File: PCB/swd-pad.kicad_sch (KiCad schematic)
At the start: 10 parts, among them J7 OroConn6p

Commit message: re-annotate schematic
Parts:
- renumbered D12 to D4, D13 to D5, D15 to D7
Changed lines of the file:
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@@
   (symbol (lib_id "SamacSys_Parts:RCLAMP3552T.TNT") (at 135.89 115.57 180) (unit 1)
     (in_bom yes) (on_board yes) (dnp no) (fields_autoplaced)
-    (property "Reference" "D13" (at 125.73 107.5309 0)
+    (property "Reference" "D5" (at 125.73 107.5309 0)
       (effects (font (size 1.27 1.27)))
     )
@@
       (project "OroLink"
         (path "/e89dcd22-1250-4a5b-b778-1c95a0dd623d/259c9346-7ad9-40c3-9e14-9b19afc78ddf"
-          (reference "D13") (unit 1)
+          (reference "D5") (unit 1)
         )
       )
@@
         )
         (path "/e89dcd22-1250-4a5b-b778-1c95a0dd623d/259c9346-7ad9-40c3-9e14-9b19afc78ddf"
-          (reference "D14") (unit 1)
+          (reference "D6") (unit 1)
         )
       )
@@
   (symbol (lib_id "power:GNDPWR") (at 111.125 115.57 0) (unit 1)
     (in_bom yes) (on_board yes) (dnp no)
-    (property "Reference" "#PWR069" (at 111.125 120.65 0)
+    (property "Reference" "#PWR072" (at 111.125 120.65 0)
       (effects (font (size 1.27 1.27)) hide)
     )
@@
       (project "OroLink"
         (path "/e89dcd22-1250-4a5b-b778-1c95a0dd623d/259c9346-7ad9-40c3-9e14-9b19afc78ddf"
-          (reference "#PWR069") (unit 1)
+          (reference "#PWR072") (unit 1)
         )
       )
@@
         )
         (path "/e89dcd22-1250-4a5b-b778-1c95a0dd623d/259c9346-7ad9-40c3-9e14-9b19afc78ddf"
-          (reference "DBG42") (unit 1)
+          (reference "DBG10") (unit 1)
         )
       )
@@
         )
         (path "/e89dcd22-1250-4a5b-b778-1c95a0dd623d/259c9346-7ad9-40c3-9e14-9b19afc78ddf"
-          (reference "#PWR070") (unit 1)
+          (reference "#PWR073") (unit 1)
         )
       )
@@
         )
         (path "/e89dcd22-1250-4a5b-b778-1c95a0dd623d/259c9346-7ad9-40c3-9e14-9b19afc78ddf"
-          (reference "DBG43") (unit 1)
+          (reference "DBG11") (unit 1)
         )
       )
@@
   (symbol (lib_id "power:GND") (at 170.18 82.55 0) (unit 1)
     (in_bom yes) (on_board yes) (dnp no) (fields_autoplaced)
-    (property "Reference" "#PWR071" (at 170.18 88.9 0)
+    (property "Reference" "#PWR074" (at 170.18 88.9 0)
       (effects (font (size 1.27 1.27)) hide)
     )
@@
       (project "OroLink"
         (path "/e89dcd22-1250-4a5b-b778-1c95a0dd623d/259c9346-7ad9-40c3-9e14-9b19afc78ddf"
-          (reference "#PWR071") (unit 1)
+          (reference "#PWR074") (unit 1)
         )
       )
@@
         )
         (path "/e89dcd22-1250-4a5b-b778-1c95a0dd623d/259c9346-7ad9-40c3-9e14-9b19afc78ddf"
-          (reference "DBG41") (unit 1)
+          (reference "DBG9") (unit 1)
         )
       )
@@
   (symbol (lib_id "power:GNDPWR") (at 188.595 115.57 0) (unit 1)
     (in_bom yes) (on_board yes) (dnp no)
-    (property "Reference" "#PWR072" (at 188.595 120.65 0)
+    (property "Reference" "#PWR075" (at 188.595 120.65 0)
       (effects (font (size 1.27 1.27)) hide)
     )
@@
       (project "OroLink"
         (path "/e89dcd22-1250-4a5b-b778-1c95a0dd623d/259c9346-7ad9-40c3-9e14-9b19afc78ddf"
-          (reference "#PWR072") (unit 1)
+          (reference "#PWR075") (unit 1)
         )
       )
@@
   (symbol (lib_id "SamacSys_Parts:RCLAMP3552T.TNT") (at 163.83 113.03 0) (unit 1)
     (in_bom yes) (on_board yes) (dnp no) (fields_autoplaced)
-    (property "Reference" "D15" (at 173.99 107.5309 0)
+    (property "Reference" "D7" (at 173.99 107.5309 0)
       (effects (font (size 1.27 1.27)))
     )
@@
       (project "OroLink"
         (path "/e89dcd22-1250-4a5b-b778-1c95a0dd623d/259c9346-7ad9-40c3-9e14-9b19afc78ddf"
-          (reference "D15") (unit 1)
+          (reference "D7") (unit 1)
         )
       )
@@
         )
         (path "/e89dcd22-1250-4a5b-b778-1c95a0dd623d/259c9346-7ad9-40c3-9e14-9b19afc78ddf"
-          (reference "DBG39") (unit 1)
+          (reference "DBG7") (unit 1)
         )
       )
@@
         )
         (path "/e89dcd22-1250-4a5b-b778-1c95a0dd623d/259c9346-7ad9-40c3-9e14-9b19afc78ddf"
-          (reference "DBG40") (unit 1)
+          (reference "DBG8") (unit 1)
         )
       )
@@
   (symbol (lib_id "power:+5V") (at 86.995 82.55 0) (unit 1)
     (in_bom yes) (on_board yes) (dnp no) (fields_autoplaced)
-    (property "Reference" "#PWR068" (at 86.995 86.36 0)
+    (property "Reference" "#PWR071" (at 86.995 86.36 0)
       (effects (font (size 1.27 1.27)) hide)
     )
@@
       (project "OroLink"
         (path "/e89dcd22-1250-4a5b-b778-1c95a0dd623d/259c9346-7ad9-40c3-9e14-9b19afc78ddf"
-          (reference "#PWR068") (unit 1)
+          (reference "#PWR071") (unit 1)
         )
       )
@@
   (symbol (lib_id "SamacSys_Parts:RFU02VSM8STR") (at 92.71 82.55 0) (unit 1)
     (in_bom yes) (on_board yes) (dnp no)
-    (property "Reference" "D12" (at 100.33 76.835 0)
+    (property "Reference" "D4" (at 100.33 76.835 0)
       (effects (font (size 1.27 1.27)))
     )
@@
       (project "OroLink"
         (path "/e89dcd22-1250-4a5b-b778-1c95a0dd623d/259c9346-7ad9-40c3-9e14-9b19afc78ddf"
-          (reference "D12") (unit 1)
-        )
-      )
+          (reference "D4") (unit 1)
+        )
+      )

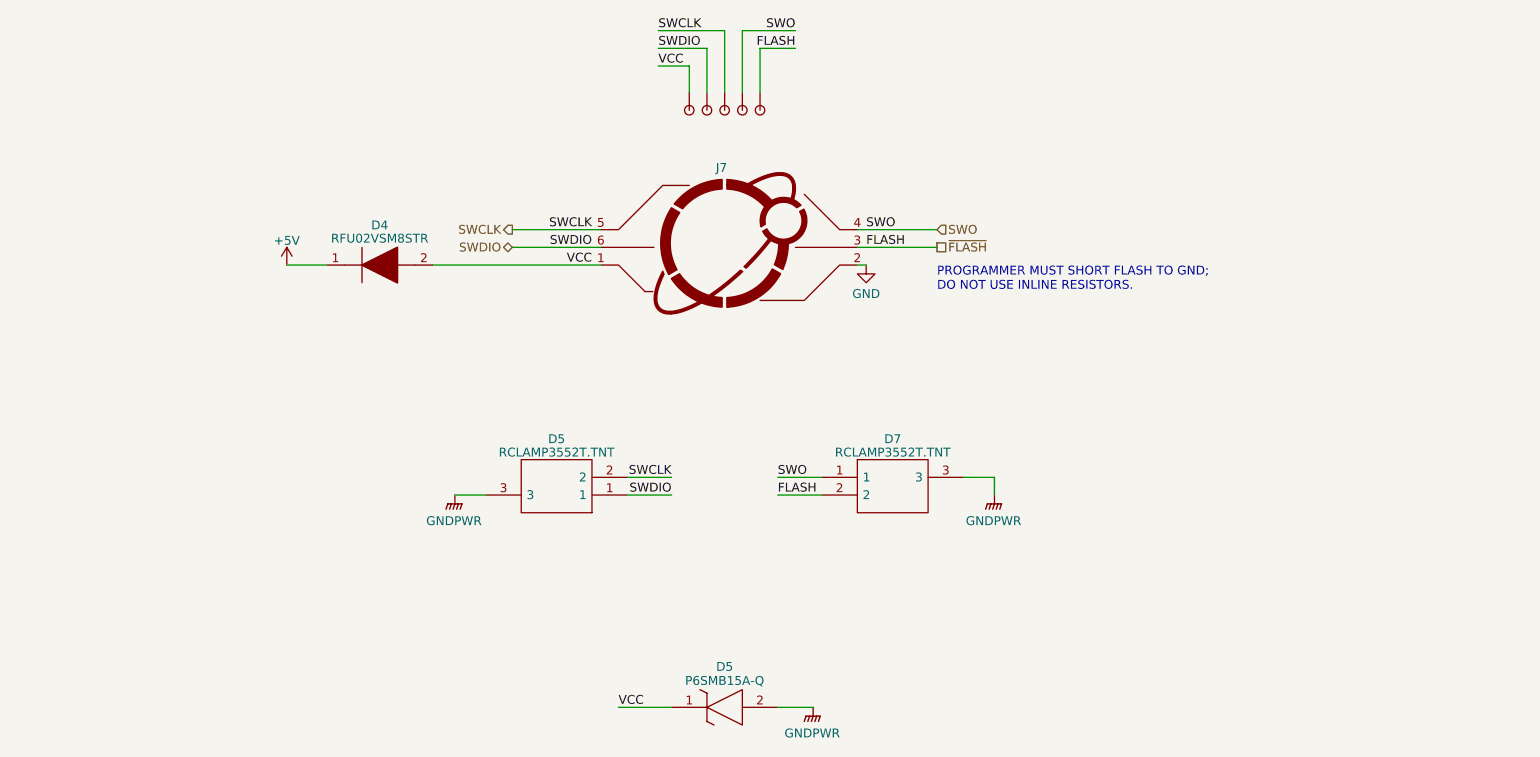
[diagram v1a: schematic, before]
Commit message: add pullup/down resistors and fix oro 6p lines with boot1/0
closes #24
closes #21
closes #15
closes #12
closes #6
closes #3
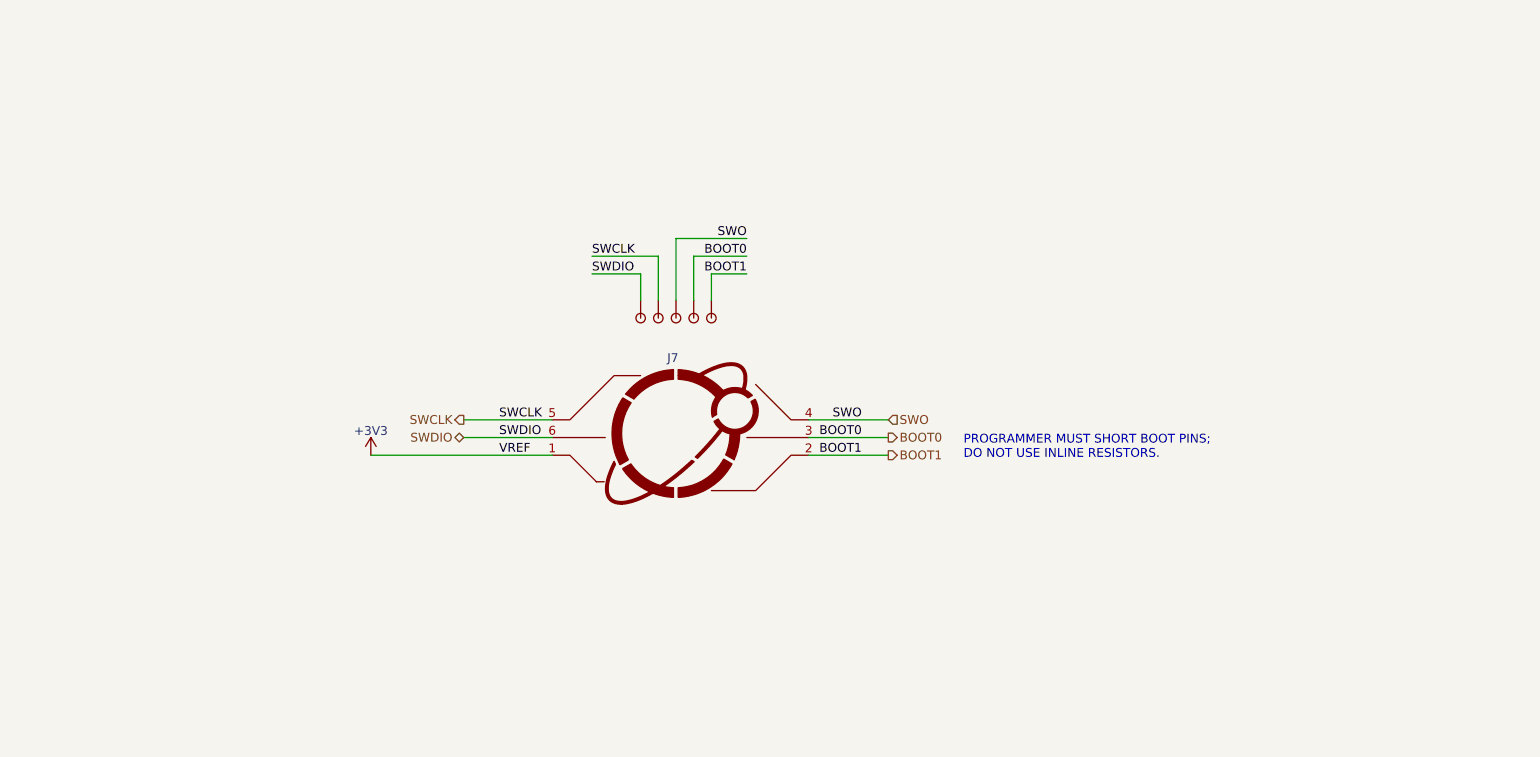
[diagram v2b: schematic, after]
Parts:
- removed D4: RFU02VSM8STR, SODFL2514X80N, symbol SamacSys_Parts:RFU02VSM8STR
- removed D5, D7: RCLAMP3552T.TNT, RCLAMP3552TTNT, symbol SamacSys_Parts:RCLAMP3552T.TNT
- removed D5: P6SMB15A-Q, DIOM5436X244N, symbol SamacSys_Parts:P6SMB15A-Q
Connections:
- net GND renamed BOOT1
- net BOOT1: now also DBG1.1
- net VCC renamed +3V3
- net +3V3: no longer DBG1.1
- net ~{FLASH} renamed BOOT0
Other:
- note added: "PROGRAMMER MUST SHORT BOOT PINS; DO NOT USE INLINE RESISTORS."
- note removed: "PROGRAMMER MUST SHORT FLASH TO GND; DO NOT USE INLINE RESISTORS."
- moved on the sheet: J7

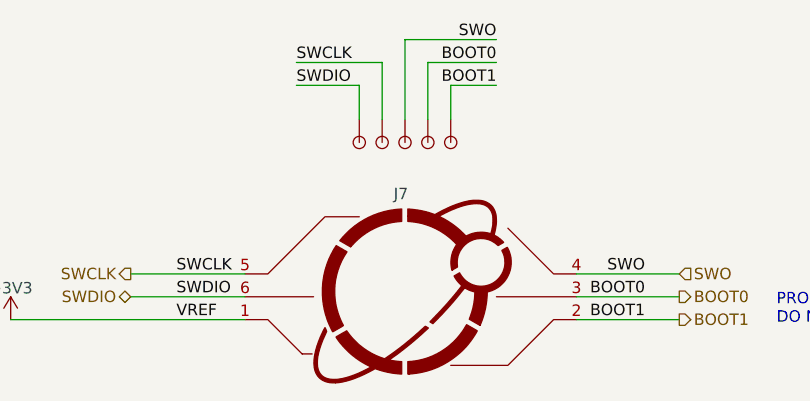
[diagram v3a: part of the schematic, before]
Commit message: preliminary routing completed
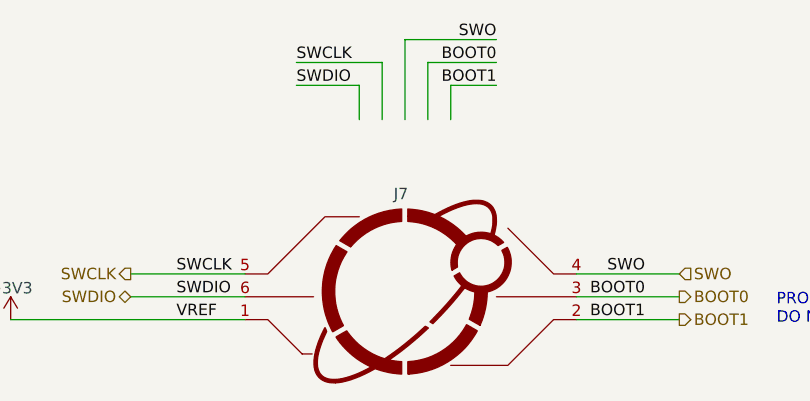
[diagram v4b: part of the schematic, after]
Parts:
- removed DBG1 (x5): ~, Oro Footprints:DebugPin, symbol Oro:DebugPin
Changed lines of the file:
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@@
     (effects (font (size 1.27 1.27)) (justify left))
-  )
-  (symbol (lib_id "Oro:DebugPin") (at 142.875 87.63 270) (unit 1)
-    (in_bom no) (on_board yes) (dnp no)
-    (property "Reference" "DBG1" (at 145.415 92.075 90)
-      (effects (font (size 1.27 1.27)) (justify right) hide)
-    )
-    (property "Value" "~" (at 142.875 87.63 0)
-      (effects (font (size 1.27 1.27)) hide)
-    )
-    (property "Footprint" "Oro Footprints:DebugPin" (at 145.415 88.9 0)
-      (effects (font (size 1.27 1.27)) hide)
-    )
-    (property "Datasheet" "" (at 142.875 87.63 0)
-      (effects (font (size 1.27 1.27)) hide)
-    )
-    (property "Sim.Enable" "0" (at 145.415 101.6 0)
-      (effects (font (size 1.27 1.27)) hide)
-    )
-    (pin "1")
-    (instances
-      (project "OroLink"
-        (path "/e89dcd22-1250-4a5b-b778-1c95a0dd623d/f955395e-bf1a-4ef3-9cfe-ec9d49f66988"
-          (reference "DBG1") (unit 1)
-        )
-        (path "/e89dcd22-1250-4a5b-b778-1c95a0dd623d/dd173832-34f8-47c0-be66-f527d6e2d134"
-          (reference "DBG8") (unit 1)
-        )
-        (path "/e89dcd22-1250-4a5b-b778-1c95a0dd623d/1b3eede1-74b0-4c0b-b4f1-7ec1bfc1f54f"
-          (reference "DBG12") (unit 1)
-        )
-        (path "/e89dcd22-1250-4a5b-b778-1c95a0dd623d/259c9346-7ad9-40c3-9e14-9b19afc78ddf"
-          (reference "DBG26") (unit 1)
-        )
-      )
-    )
   )
   (symbol (lib_id "Oro:OroConn6p") (at 142.875 106.045 0) (unit 1)
@@
     )
   )
-  (symbol (lib_id "Oro:DebugPin") (at 145.415 87.63 270) (unit 1)
-    (in_bom no) (on_board yes) (dnp no)
-    (property "Reference" "DBG1" (at 147.955 92.075 90)
-      (effects (font (size 1.27 1.27)) (justify right) hide)
-    )
-    (property "Value" "~" (at 145.415 87.63 0)
-      (effects (font (size 1.27 1.27)) hide)
-    )
-    (property "Footprint" "Oro Footprints:DebugPin" (at 147.955 88.9 0)
-      (effects (font (size 1.27 1.27)) hide)
-    )
-    (property "Datasheet" "" (at 145.415 87.63 0)
-      (effects (font (size 1.27 1.27)) hide)
-    )
-    (property "Sim.Enable" "0" (at 147.955 101.6 0)
-      (effects (font (size 1.27 1.27)) hide)
-    )
-    (pin "1")
-    (instances
-      (project "OroLink"
-        (path "/e89dcd22-1250-4a5b-b778-1c95a0dd623d/f955395e-bf1a-4ef3-9cfe-ec9d49f66988"
-          (reference "DBG1") (unit 1)
-        )
-        (path "/e89dcd22-1250-4a5b-b778-1c95a0dd623d/dd173832-34f8-47c0-be66-f527d6e2d134"
-          (reference "DBG8") (unit 1)
-        )
-        (path "/e89dcd22-1250-4a5b-b778-1c95a0dd623d/1b3eede1-74b0-4c0b-b4f1-7ec1bfc1f54f"
-          (reference "DBG12") (unit 1)
-        )
-        (path "/e89dcd22-1250-4a5b-b778-1c95a0dd623d/259c9346-7ad9-40c3-9e14-9b19afc78ddf"
-          (reference "DBG27") (unit 1)
-        )
-      )
-    )
-  )
-  (symbol (lib_id "Oro:DebugPin") (at 140.335 87.63 270) (unit 1)
-    (in_bom no) (on_board yes) (dnp no)
-    (property "Reference" "DBG1" (at 142.875 92.075 90)
-      (effects (font (size 1.27 1.27)) (justify right) hide)
-    )
-    (property "Value" "~" (at 140.335 87.63 0)
-      (effects (font (size 1.27 1.27)) hide)
-    )
-    (property "Footprint" "Oro Footprints:DebugPin" (at 142.875 88.9 0)
-      (effects (font (size 1.27 1.27)) hide)
-    )
-    (property "Datasheet" "" (at 140.335 87.63 0)
-      (effects (font (size 1.27 1.27)) hide)
-    )
-    (property "Sim.Enable" "0" (at 142.875 101.6 0)
-      (effects (font (size 1.27 1.27)) hide)
-    )
-    (pin "1")
-    (instances
-      (project "OroLink"
-        (path "/e89dcd22-1250-4a5b-b778-1c95a0dd623d/f955395e-bf1a-4ef3-9cfe-ec9d49f66988"
-          (reference "DBG1") (unit 1)
-        )
-        (path "/e89dcd22-1250-4a5b-b778-1c95a0dd623d/dd173832-34f8-47c0-be66-f527d6e2d134"
-          (reference "DBG8") (unit 1)
-        )
-        (path "/e89dcd22-1250-4a5b-b778-1c95a0dd623d/1b3eede1-74b0-4c0b-b4f1-7ec1bfc1f54f"
-          (reference "DBG12") (unit 1)
-        )
-        (path "/e89dcd22-1250-4a5b-b778-1c95a0dd623d/259c9346-7ad9-40c3-9e14-9b19afc78ddf"
-          (reference "DBG25") (unit 1)
-        )
-      )
-    )
-  )
-  (symbol (lib_id "Oro:DebugPin") (at 137.795 87.63 270) (unit 1)
-    (in_bom no) (on_board yes) (dnp no)
-    (property "Reference" "DBG1" (at 140.335 92.075 90)
-      (effects (font (size 1.27 1.27)) (justify right) hide)
-    )
-    (property "Value" "~" (at 137.795 87.63 0)
-      (effects (font (size 1.27 1.27)) hide)
-    )
-    (property "Footprint" "Oro Footprints:DebugPin" (at 140.335 88.9 0)
-      (effects (font (size 1.27 1.27)) hide)
-    )
-    (property "Datasheet" "" (at 137.795 87.63 0)
-      (effects (font (size 1.27 1.27)) hide)
-    )
-    (property "Sim.Enable" "0" (at 140.335 101.6 0)
-      (effects (font (size 1.27 1.27)) hide)
-    )
-    (pin "1")
-    (instances
-      (project "OroLink"
-        (path "/e89dcd22-1250-4a5b-b778-1c95a0dd623d/f955395e-bf1a-4ef3-9cfe-ec9d49f66988"
-          (reference "DBG1") (unit 1)
-        )
-        (path "/e89dcd22-1250-4a5b-b778-1c95a0dd623d/dd173832-34f8-47c0-be66-f527d6e2d134"
-          (reference "DBG8") (unit 1)
-        )
-        (path "/e89dcd22-1250-4a5b-b778-1c95a0dd623d/1b3eede1-74b0-4c0b-b4f1-7ec1bfc1f54f"
-          (reference "DBG12") (unit 1)
-        )
-        (path "/e89dcd22-1250-4a5b-b778-1c95a0dd623d/259c9346-7ad9-40c3-9e14-9b19afc78ddf"
-          (reference "DBG24") (unit 1)
-        )
-      )
-    )
-  )
   (symbol (lib_id "power:+3V3") (at 99.06 109.855 0) (unit 1)
     (in_bom yes) (on_board yes) (dnp no) (fields_autoplaced)
@@
         )
       )
-    )
-  )
-  (symbol (lib_id "Oro:DebugPin") (at 147.955 87.63 270) (unit 1)
-    (in_bom no) (on_board yes) (dnp no)
-    (property "Reference" "DBG1" (at 150.495 92.075 90)
-      (effects (font (size 1.27 1.27)) (justify right) hide)
-    )
-    (property "Value" "~" (at 147.955 87.63 0)
-      (effects (font (size 1.27 1.27)) hide)
-    )
-    (property "Footprint" "Oro Footprints:DebugPin" (at 150.495 88.9 0)
-      (effects (font (size 1.27 1.27)) hide)
-    )
-    (property "Datasheet" "" (at 147.955 87.63 0)
-      (effects (font (size 1.27 1.27)) hide)
-    )
-    (property "Sim.Enable" "0" (at 150.495 101.6 0)
-      (effects (font (size 1.27 1.27)) hide)
-    )
-    (pin "1")
-    (instances
-      (project "OroLink"
-        (path "/e89dcd22-1250-4a5b-b778-1c95a0dd623d/f955395e-bf1a-4ef3-9cfe-ec9d49f66988"
-          (reference "DBG1") (unit 1)
-        )
-        (path "/e89dcd22-1250-4a5b-b778-1c95a0dd623d/dd173832-34f8-47c0-be66-f527d6e2d134"
-          (reference "DBG8") (unit 1)
-        )
-        (path "/e89dcd22-1250-4a5b-b778-1c95a0dd623d/1b3eede1-74b0-4c0b-b4f1-7ec1bfc1f54f"
-          (reference "DBG12") (unit 1)
-        )
-        (path "/e89dcd22-1250-4a5b-b778-1c95a0dd623d/259c9346-7ad9-40c3-9e14-9b19afc78ddf"
-          (reference "DBG28") (unit 1)
-        )
-      )
